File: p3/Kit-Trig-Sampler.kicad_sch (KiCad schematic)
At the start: 81 parts, among them J1 START_CV, J10 AUDIO_INR, J11 AUDIO_OUTL, J13 BANK_CV, J14 Eurorack_Power_10pin_Unshroud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, J2 LENGTH_CV, J3 SAMP_CV, J4 PITCH CV, J5 REV_TRIG, J6 PLAY_TRIG, J7 END_OUT, J8 AUDIO_INL, J9 AUIDO_OUTR, U1 TL082_TH, U2 TL082_TH, U3 78M33_TH

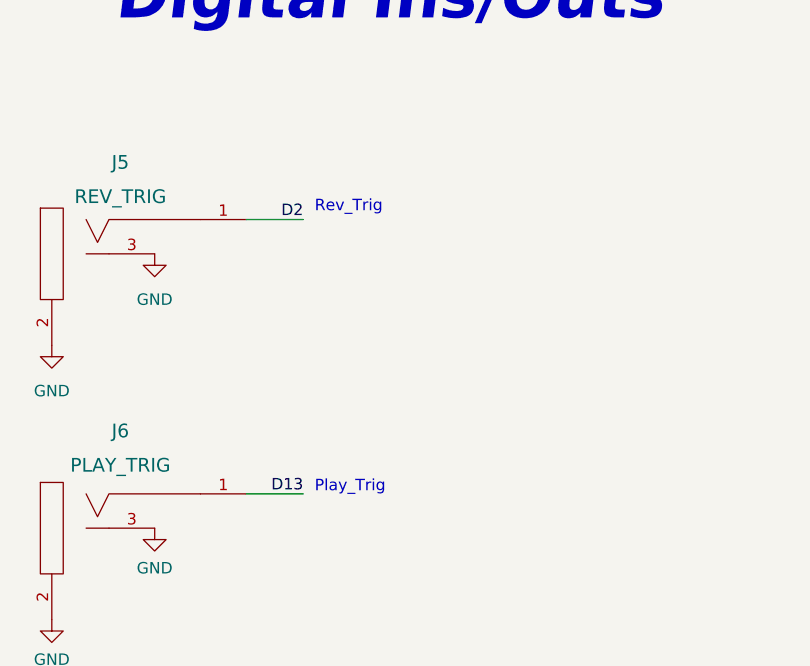
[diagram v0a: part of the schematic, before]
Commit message: p3: added 47k resistors to Trig Ins
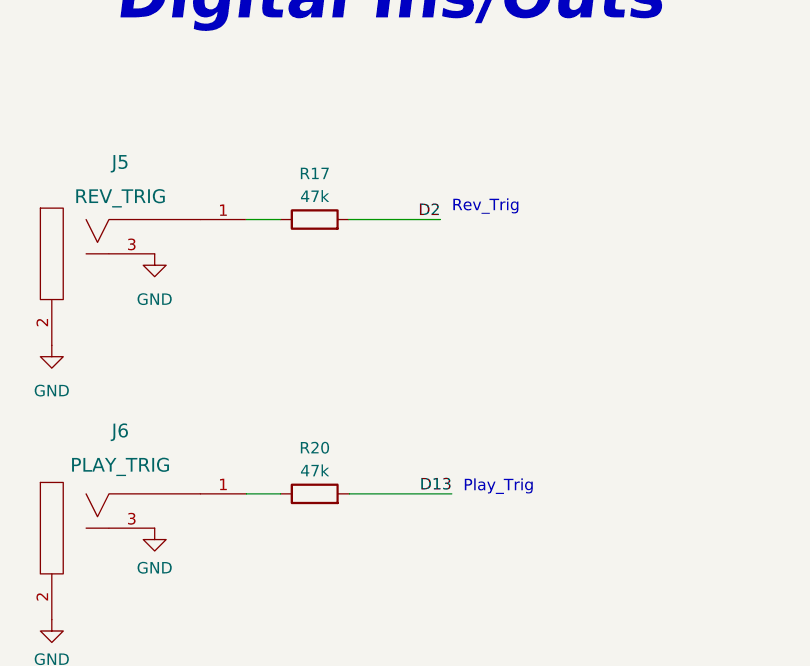
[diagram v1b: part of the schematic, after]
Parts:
- added R17, R20: 47k_TH0.125, 4ms_Resistor:R_Axial_DIN0207_L6.3mm_D2.5mm_P7.62mm_Horizontal, symbol 4ms_Resistor_TH:47k_TH0.125
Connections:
- net D13: now also R20.2; no longer J6.1 (SIG)
- net D2: now also R17.2; no longer J5.1 (SIG)
- new net: J6.1 (SIG), R20.1
- new net: J5.1 (SIG), R17.1
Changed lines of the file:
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@@
     (stroke (width 0) (type default))
   )
+  (wire (pts (xy 205.74 49.53) (xy 215.9 49.53))
+    (stroke (width 0) (type default))
+  )
   (wire (pts (xy 82.55 210.82) (xy 85.09 210.82))
     (stroke (width 0) (type default))
@@
     (stroke (width 0) (type default))
   )
+  (wire (pts (xy 205.74 80.01) (xy 217.17 80.01))
+    (stroke (width 0) (type default))
+  )
   (wire (pts (xy 375.92 214.63) (xy 379.73 214.63))
     (stroke (width 0) (type default))
@@
     (stroke (width 0) (type default))
   )
-  (wire (pts (xy 194.31 80.01) (xy 200.66 80.01))
+  (wire (pts (xy 194.31 80.01) (xy 198.12 80.01))
     (stroke (width 0) (type default))
   )
@@
     (stroke (width 0) (type default))
   )
-  (wire (pts (xy 194.31 49.53) (xy 200.66 49.53))
+  (wire (pts (xy 194.31 49.53) (xy 198.12 49.53))
     (stroke (width 0) (type default))
   )
@@
     (stroke (width 0) (type default))
   )
-  (text "Rev_Trig" (at 201.93 48.895 0)
+  (text "Rev_Trig" (at 217.17 48.895 0)
     (effects (font (size 1.27 1.27)) (justify left bottom))
   )
@@
     (effects (font (size 1.27 1.27)) (justify left bottom))
   )
-  (text "Play_Trig" (at 201.93 80.01 0)
+  (text "Play_Trig" (at 218.44 80.01 0)
     (effects (font (size 1.27 1.27)) (justify left bottom))
   )
@@
     (effects (font (size 1.27 1.27)) (justify right bottom))
   )
-  (label "D2" (at 200.66 49.53 180) (fields_autoplaced)
+  (label "D2" (at 215.9 49.53 180) (fields_autoplaced)
     (effects (font (size 1.27 1.27)) (justify right bottom))
   )
@@
     (effects (font (size 1.27 1.27)) (justify left bottom))
   )
-  (label "D13" (at 200.66 80.01 180) (fields_autoplaced)
+  (label "D13" (at 217.17 80.01 180) (fields_autoplaced)
     (effects (font (size 1.27 1.27)) (justify right bottom))
   )
@@
     )
   )
+  (symbol (lib_id "4ms_Resistor_TH:47k_TH0.125") (at 201.93 80.01 90) (unit 1)
+    (in_bom yes) (on_board yes) (dnp no) (fields_autoplaced)
+    (property "Reference" "R20" (at 201.93 74.93 90)
+      (effects (font (size 1.27 1.27)))
+    )
+    (property "Value" "47k_TH0.125" (at 201.93 82.55 90)
+      (effects (font (size 1.27 1.27)) hide)
+    )
+    (property "Footprint" "4ms_Resistor:R_Axial_DIN0207_L6.3mm_D2.5mm_P7.62mm_Horizontal" (at 214.63 82.55 0)
+      (effects (font (size 1.27 1.27)) (justify left) hide)
+    )
+    (property "Datasheet" "" (at 201.93 80.01 0)
+      (effects (font (size 1.27 1.27)) hide)
+    )
+    (property "Specifications" "47k, 5%, 1/8W, TH0.125" (at 209.804 82.55 0)
+      (effects (font (size 1.27 1.27)) (justify left) hide)
+    )
+    (property "Manufacturer" "Xicon" (at 211.328 82.55 0)
+      (effects (font (size 1.27 1.27)) (justify left) hide)
+    )
+    (property "Part Number" "299-47k-RC" (at 212.852 82.55 0)
+      (effects (font (size 1.27 1.27)) (justify left) hide)
+    )
+    (property "Display" "47k" (at 201.93 77.47 90)
+      (effects (font (size 1.27 1.27)))
+    )
+    (property "JLCPCB ID" "" (at 201.93 76.2 90)
+      (effects (font (size 1.27 1.27)) hide)
+    )
+    (pin "1")
+    (pin "2")
+    (instances
+      (project "Kit-Trig-Sampler"
+        (path "/39a72d2b-4494-42c9-aa7a-6ac21ca5673f"
+          (reference "R20") (unit 1)
+        )
+      )
+    )
+  )
   (symbol (lib_id "4ms_Power-symbol:GND") (at 350.52 387.35 0) (unit 1)
     (in_bom yes) (on_board yes) (dnp no) (fields_autoplaced)
@@
         )
       )
+    )
+  )
+  (symbol (lib_id "4ms_Resistor_TH:47k_TH0.125") (at 201.93 49.53 90) (unit 1)
+    (in_bom yes) (on_board yes) (dnp no) (fields_autoplaced)
+    (property "Reference" "R17" (at 201.93 44.45 90)
+      (effects (font (size 1.27 1.27)))
+    )
+    (property "Value" "47k_TH0.125" (at 201.93 52.07 90)
+      (effects (font (size 1.27 1.27)) hide)
+    )
+    (property "Footprint" "4ms_Resistor:R_Axial_DIN0207_L6.3mm_D2.5mm_P7.62mm_Horizontal" (at 214.63 52.07 0)
+      (effects (font (size 1.27 1.27)) (justify left) hide)
+    )
+    (property "Datasheet" "" (at 201.93 49.53 0)
+      (effects (font (size 1.27 1.27)) hide)
+    )
+    (property "Specifications" "47k, 5%, 1/8W, TH0.125" (at 209.804 52.07 0)
+      (effects (font (size 1.27 1.27)) (justify left) hide)
+    )
+    (property "Manufacturer" "Xicon" (at 211.328 52.07 0)
+      (effects (font (size 1.27 1.27)) (justify left) hide)
+    )
+    (property "Part Number" "299-47k-RC" (at 212.852 52.07 0)
+      (effects (font (size 1.27 1.27)) (justify left) hide)
+    )
+    (property "Display" "47k" (at 201.93 46.99 90)
+      (effects (font (size 1.27 1.27)))
+    )
+    (property "JLCPCB ID" "" (at 201.93 45.72 90)
+      (effects (font (size 1.27 1.27)) hide)
+    )
+    (pin "1")
+    (pin "2")
+    (instances
+      (project "Kit-Trig-Sampler"
+        (path "/39a72d2b-4494-42c9-aa7a-6ac21ca5673f"
+          (reference "R17") (unit 1)
+        )
+      )

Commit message: updating sch with BOM info
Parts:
- C1, C10, C12, C13, C14, C15, C16, C17, C2, C3, C7, C8, C9: Manufacturer (none) -> Vishay; Part Number (none) -> K104Z15Y5VF53L2; Production Stage (none) -> B; Specifications (none) -> MLCC, Leaded, Min 25V, Y5V, Lead Spacing 2.5mm, Body approx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
- C11: Manufacturer (none) -> Vishay; Part Number (none) -> D101K20Y5PL6TJ5R; Production Stage (none) -> B; Specifications (none) -> Ceramic Disc, Max 20% tolerance, 5mm Lead Spacing, 5mm Diam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
- C19, C20, C4, C5: Display 47uF/16V -> 47uF; Manufacturer (none) -> Panasonic; Manufacturer 2 (none) -> Lelon; Part Number (none) -> ECA-1VM470I; Part Number 2 (none) -> RGA470M1VBK-0611G; Production Stage (none) -> B; Specifications 47uF, 16V -> Aluminum Electrolytic, Radial Leaded, Min 25V, 5mm Diameter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
- C6: JLCPCB ID C163508 -> (none); Manufacturer Murata -> Nichicon; Part Number GRM1885C1H102JA01D -> QYX2A102KTP1FD; Production Stage (none) -> B; Specifications 1nF, 50V, 10%, C0G (NP0) or similar -> Film Capacitor, Min 25V, Max 20% tolerance, Lead Spacing 5m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
- JA1, JB1, JC1, JD1: value Socket_02x05_TH -> Socket_02x05_P2.54mm_TH; symbol 4ms_Connector:Socket_02x05_TH -> 4ms_Connector:Socket_02x05_P2.54mm_TH; Manufacturer (none) -> Samtec; Part Number (none) -> SSW-105-01-G-D; Production Stage (none) -> B; Specifications HEADER 2x5 FEMALE PINS 0.100” 180deg -> HEADER 2x5 FEMALE SOCKET 0.100” 180deg
- R11: value 1k_TH0.125 -> 33k_TH0.125
- R27: value 10k_TH0.125 -> 47k_TH0.125

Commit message: Update instructions.pdf, update BOM, export Gerbers
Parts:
- added FP1: Faceplate, symbol 4ms_Hardware:Faceplate
- added KNOB1, KNOB2, KNOB3, KNOB4: Davies D-shaft, symbol 4ms_Hardware:Knob_Davies_WhiteLine
- added PCB1: PCB, symbol 4ms_Hardware:PCB
- added SK1, SK2: DIP-8 socket, symbol 4ms_Connector:Socket_DIP8
- added U4: STS SD card w/adaptor, symbol 4ms_Hardware:microSDcard_STS
- Bank_But1, PLAY_BUT1, POT_LENGTH1, POT_PITCH1, POT_SAMP1, POT_START1, REV_BUT1, SD1: Production Stage (none) -> C
- D1, D2, J14, R1, R10, R11, R12, R13, R14, R15, R16, R17, R18, R19, R2, R20, R21, R23, R25, R26, R27, R28, R3, R30, R31, R32, R33, R34, R37, R4, R40, R41, R5, R6, R7, R8, R9: Production Stage (none) -> B
- J1: value START_CV -> 3.5mm_Mono_Switched; Production Stage (none) -> C
- J10: value AUDIO_INR -> 3.5mm_Mono_Switched; Production Stage (none) -> C
- J11: value AUDIO_OUTL -> 3.5mm_Mono_Switched; Production Stage (none) -> C
- J13: value BANK_CV -> 3.5mm_Mono_Switched; Production Stage (none) -> C
- J2: value LENGTH_CV -> 3.5mm_Mono_Switched; Production Stage (none) -> C
- J3: value SAMP_CV -> 3.5mm_Mono_Switched; Production Stage (none) -> C
- J4: value PITCH CV -> 3.5mm_Mono_Switched; Production Stage (none) -> C
- J5: value REV_TRIG -> 3.5mm_Mono_Switched; Production Stage (none) -> C
- J6: value PLAY_TRIG -> 3.5mm_Mono_Switched; Production Stage (none) -> C
- J7: value END_OUT -> 3.5mm_Mono_Switched; Production Stage (none) -> C
- J8: value AUDIO_INL -> 3.5mm_Mono_Switched; Production Stage (none) -> C
- J9: value AUIDO_OUTR -> 3.5mm_Mono_Switched; Production Stage (none) -> C
- U1, U2: value TL082_TH -> TL072_TH; symbol 4ms_IC:TL082_TH -> 4ms_IC:TL072_TH; Manufacturer (none) -> Texas Instruments; Part Number (none) -> TL072IP; Production Stage (none) -> B; Specifications TL082 Dual Opamp DIP-8pin -> Dual Opamp DIP-8 JFET Input, Low Noise, Min 24Vpp Vsupply, 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
- U3: Manufacturer (none) -> TBD; Part Number (none) -> TBD; Production Stage (none) -> B; Specifications (none) -> Voltage Regulator, Vout = 3.3V, Vin(min) > 12V, Imax > 100m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

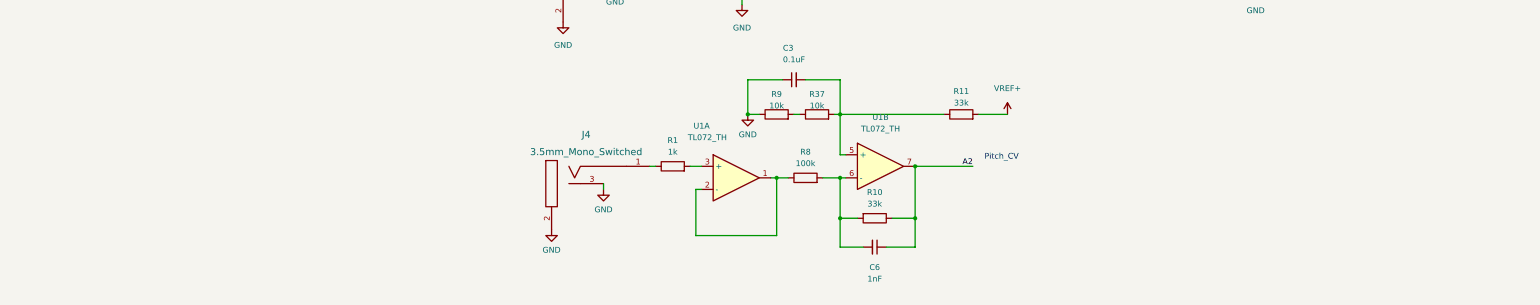
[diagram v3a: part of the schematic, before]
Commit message: p3: Change Pitch CV range: R9=>47k. Deleted R37
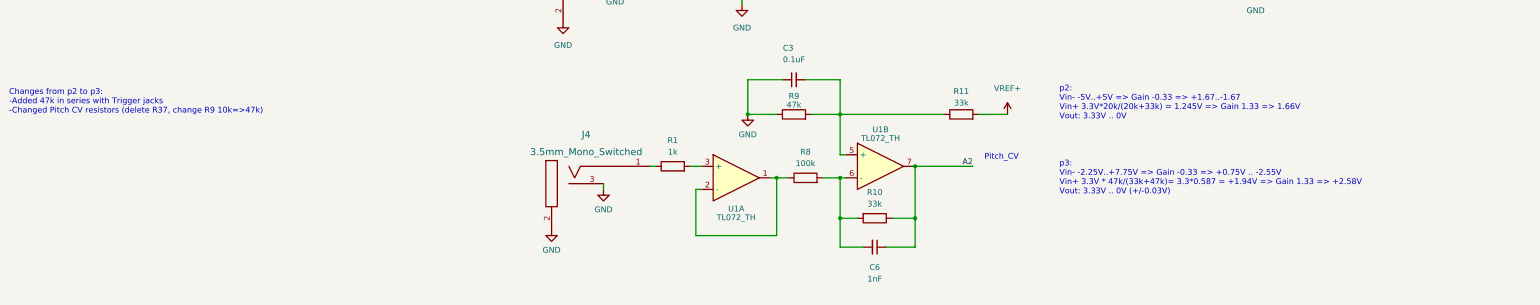
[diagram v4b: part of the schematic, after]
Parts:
- removed R37: 10k_TH0.125, 4ms_Resistor:R_Axial_DIN0207_L6.3mm_D2.5mm_P7.62mm_Horizontal, symbol 4ms_Resistor_TH:10k_TH0.125
- R9: value 10k_TH0.125 -> 47k_TH0.125; symbol 4ms_Resistor_TH:10k_TH0.125 -> 4ms_Resistor_TH:47k_TH0.125; Display 10k -> 47k; Part Number 299-10k-RC -> 299-47k-RC; Production Stage B -> (none); Specifications 10k, 5%, 1/8W, TH0.125 -> 47k, 5%, 1/8W, TH0.125
- U3: Manufacturer TBD -> Diodes Incorporated; Part Number TBD -> AP7381-33V-A
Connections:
- net at R9.2: now also C3.2, R11.1, U1.5 (+)
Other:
- note added: "Changes from p2 to p3: -Added 47k in series with Trigger jacks -Changed Pitch CV resistors (delete R37, change R9 10k=>47k)"
- note added: "p2: Vin- -5V..+5V => Gain -0.33 => +1.67..-1.67 Vin+ 3.3V*20k/(20k+33k) = 1.245V => Gain 1.33 => 1.66V Vout: 3.33V .. 0V"
- note added: "p3: Vin- -2.25V..+7.75V => Gain -0.33 => +0.75V .. -2.55V Vin+ 3.3V * 47k/(33k+47k)= 3.3*0.587 = +1.94V => Gain 1.33 => +2.58V Vout: 3.33V .. 0V (+/-0.03V)"
- moved on the sheet: R9
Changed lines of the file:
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@@
     (stroke (width 0) (type default))
   )
-  (wire (pts (xy 95.25 199.39) (xy 97.79 199.39))
+  (wire (pts (xy 95.25 199.39) (xy 101.6 199.39))
     (stroke (width 0) (type default))
   )
@@
     (stroke (width 0) (type default))
   )
-  (wire (pts (xy 114.3 199.39) (xy 115.57 199.39))
-    (stroke (width 0) (type default))
-  )
   (wire (pts (xy 116.84 382.27) (xy 116.84 383.54))
     (stroke (width 0) (type default))
@@
     (stroke (width 0) (type default))
   )
-  (wire (pts (xy 105.41 199.39) (xy 106.68 199.39))
+  (wire (pts (xy 109.22 199.39) (xy 115.57 199.39))
     (stroke (width 0) (type default))
   )
@@
     (effects (font (size 1.27 1.27)) (justify left bottom))
   )
+  (text "p3:\nVin- -2.25V..+7.75V => Gain -0.33 => +0.75V .. -2.55V\nVin+ 3.3V * 47k/(33k+47k)= 3.3*0.587 = +1.94V => Gain 1.33 => +2.58V\nVout: 3.33V .. 0V (+/-0.03V)"
+    (at 163.83 217.17 0)
+    (effects (font (size 1.27 1.27)) (justify left bottom))
+  )
   (text "Sample_Pot" (at 81.915 306.07 0)
     (effects (font (size 1.27 1.27)) (justify left bottom))
@@
     (effects (font (size 1.27 1.27)) (justify right bottom))
   )
+  (text "p2:\nVin- -5V..+5V => Gain -0.33 => +1.67..-1.67\nVin+ 3.3V*20k/(20k+33k) = 1.245V => Gain 1.33 => 1.66V\nVout: 3.33V .. 0V"
+    (at 163.83 200.66 0)
+    (effects (font (size 1.27 1.27)) (justify left bottom))
+  )
   (text "4ms Sampler Kit" (at 481.33 387.35 0)
     (effects (font (size 5.08 5.08) (thickness 1.016) bold italic) (justify left bottom))
@@
     (effects (font (size 1.27 1.27)) (justify right bottom))
   )
+  (text "Changes from p2 to p3:\n-Added 47k in series with Trigger jacks\n-Changed Pitch CV resistors (delete R37, change R9 10k=>47k)"
+    (at -67.31 199.39 0)
+    (effects (font (size 1.27 1.27)) (justify left bottom))
+  )
   (text "Bank_But_B" (at 450.85 205.74 0)
     (effects (font (size 1.27 1.27)) (justify right bottom))
@@
     )
   )
-  (symbol (lib_id "4ms_Resistor_TH:10k_TH0.125") (at 101.6 199.39 90) (unit 1)
+  (symbol (lib_id "4ms_Resistor_TH:47k_TH0.125") (at 105.41 199.39 90) (unit 1)
     (in_bom yes) (on_board yes) (dnp no) (fields_autoplaced)
-    (property "Reference" "R9" (at 101.6 194.945 90)
+    (property "Reference" "R9" (at 105.41 195.3641 90)
       (effects (font (size 1.27 1.27)))
     )
-    (property "Value" "10k_TH0.125" (at 101.6 201.93 90)
+    (property "Value" "47k_TH0.125" (at 105.41 201.93 90)
       (effects (font (size 1.27 1.27)) hide)
     )
-    (property "Footprint" "4ms_Resistor:R_Axial_DIN0207_L6.3mm_D2.5mm_P7.62mm_Horizontal" (at 114.3 201.93 0)
+    (property "Footprint" "4ms_Resistor:R_Axial_DIN0207_L6.3mm_D2.5mm_P7.62mm_Horizontal" (at 118.11 201.93 0)
       (effects (font (size 1.27 1.27)) (justify left) hide)
     )
-    (property "Datasheet" "" (at 101.6 199.39 0)
+    (property "Datasheet" "" (at 105.41 199.39 0)
       (effects (font (size 1.27 1.27)) hide)
     )
-    (property "Specifications" "10k, 5%, 1/8W, TH0.125" (at 109.474 201.93 0)
+    (property "Specifications" "47k, 5%, 1/8W, TH0.125" (at 113.284 201.93 0)
       (effects (font (size 1.27 1.27)) (justify left) hide)
     )
-    (property "Manufacturer" "Xicon" (at 110.998 201.93 0)
+    (property "Manufacturer" "Xicon" (at 114.808 201.93 0)
       (effects (font (size 1.27 1.27)) (justify left) hide)
     )
-    (property "Part Number" "299-10k-RC" (at 112.522 201.93 0)
+    (property "Part Number" "299-47k-RC" (at 116.332 201.93 0)
       (effects (font (size 1.27 1.27)) (justify left) hide)
     )
-    (property "Display" "10k" (at 101.6 197.485 90)
+    (property "Display" "47k" (at 105.41 197.2851 90)
       (effects (font (size 1.27 1.27)))
     )
-    (property "JLCPCB ID" "" (at 101.6 195.58 90)
-      (effects (font (size 1.27 1.27)) hide)
-    )
-    (property "Production Stage" "B" (at 101.6 199.39 0)
+    (property "JLCPCB ID" "" (at 105.41 195.58 90)
       (effects (font (size 1.27 1.27)) hide)
     )
@@
     )
   )
-  (symbol (lib_id "4ms_Resistor_TH:10k_TH0.125") (at 110.49 199.39 90) (unit 1)
-    (in_bom yes) (on_board yes) (dnp no) (fields_autoplaced)
-    (property "Reference" "R37" (at 110.49 194.945 90)
-      (effects (font (size 1.27 1.27)))
-    )
-    (property "Value" "10k_TH0.125" (at 110.49 201.93 90)
-      (effects (font (size 1.27 1.27)) hide)
-    )
-    (property "Footprint" "4ms_Resistor:R_Axial_DIN0207_L6.3mm_D2.5mm_P7.62mm_Horizontal" (at 123.19 201.93 0)
-      (effects (font (size 1.27 1.27)) (justify left) hide)
-    )
-    (property "Datasheet" "" (at 110.49 199.39 0)
-      (effects (font (size 1.27 1.27)) hide)
-    )
-    (property "Specifications" "10k, 5%, 1/8W, TH0.125" (at 118.364 201.93 0)
-      (effects (font (size 1.27 1.27)) (justify left) hide)
-    )
-    (property "Manufacturer" "Xicon" (at 119.888 201.93 0)
-      (effects (font (size 1.27 1.27)) (justify left) hide)
-    )
-    (property "Part Number" "299-10k-RC" (at 121.412 201.93 0)
-      (effects (font (size 1.27 1.27)) (justify left) hide)
-    )
-    (property "Display" "10k" (at 110.49 197.485 90)
-      (effects (font (size 1.27 1.27)))
-    )
-    (property "JLCPCB ID" "" (at 110.49 195.58 90)
-      (effects (font (size 1.27 1.27)) hide)
-    )
-    (property "Production Stage" "B" (at 110.49 199.39 0)
-      (effects (font (size 1.27 1.27)) hide)
-    )
-    (pin "1")
-    (pin "2")
-    (instances
-      (project "Kit-Trig-Sampler"
-        (path "/39a72d2b-4494-42c9-aa7a-6ac21ca5673f"
-          (reference "R37") (unit 1)
-        )
-      )
-    )
-  )
   (symbol (lib_id "power:GND") (at 269.24 132.08 0) (unit 1)
     (in_bom yes) (on_board yes) (dnp no) (fields_autoplaced)
@@
   )
   (symbol (lib_id "4ms_IC:TL072_TH") (at 92.71 213.36 0) (unit 1)
-    (in_bom yes) (on_board yes) (dnp no)
-    (property "Reference" "U1" (at 85.09 201.93 0)
+    (in_bom yes) (on_board yes) (dnp no) (fields_autoplaced)
+    (property "Reference" "U1" (at 92.71 220.1625 0)
       (effects (font (size 1.27 1.27)))
     )
-    (property "Value" "TL072_TH" (at 86.36 204.47 0)
+    (property "Value" "TL072_TH" (at 92.71 222.0835 0)
       (effects (font (size 1.27 1.27)))
     )
@@
       (effects (font (size 1.27 1.27)) hide)
     )
-    (property "Manufacturer" "TBD" (at 364.49 382.27 0)
+    (property "Manufacturer" "Diodes Incorporated" (at 364.49 382.27 0)
       (effects (font (size 1.27 1.27)) hide)
     )
-    (property "Part Number" "TBD" (at 364.49 382.27 0)
+    (property "Part Number" "AP7381-33V-A" (at 364.49 382.27 0)
       (effects (font (size 1.27 1.27)) hide)
     )
@@
   )
   (symbol (lib_id "4ms_IC:TL072_TH") (at 124.46 210.82 0) (unit 2)
-    (in_bom yes) (on_board yes) (dnp no)
-    (property "Reference" "U1" (at 124.46 200.025 0)
+    (in_bom yes) (on_board yes) (dnp no) (fields_autoplaced)
+    (property "Reference" "U1" (at 124.46 202.7301 0)
       (effects (font (size 1.27 1.27)))
     )
-    (property "Value" "TL072_TH" (at 124.46 202.565 0)
+    (property "Value" "TL072_TH" (at 124.46 204.6511 0)
       (effects (font (size 1.27 1.27)))
     )
